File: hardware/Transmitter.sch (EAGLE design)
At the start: 2 parts, among them IC1 ATmega328P, U3 NRF24L01+

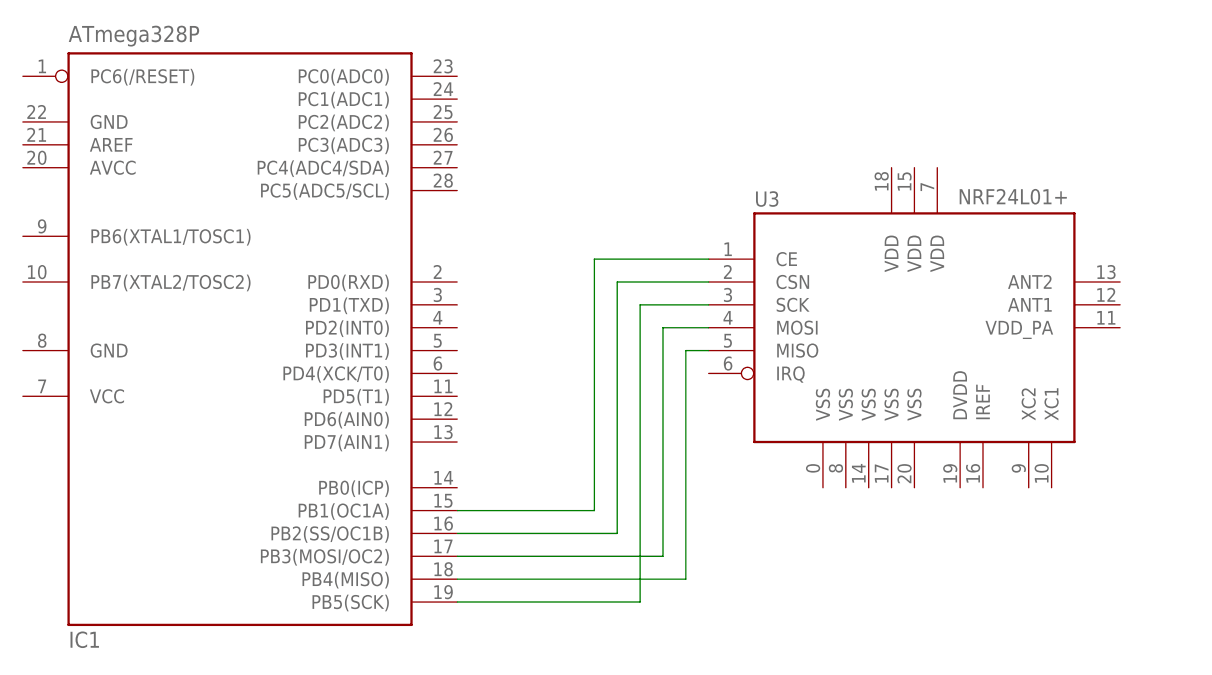
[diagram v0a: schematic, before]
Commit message: Added missing RESET/AVCC connections and eliminated short circuit in off switch
Resized schematics to conform image sizes
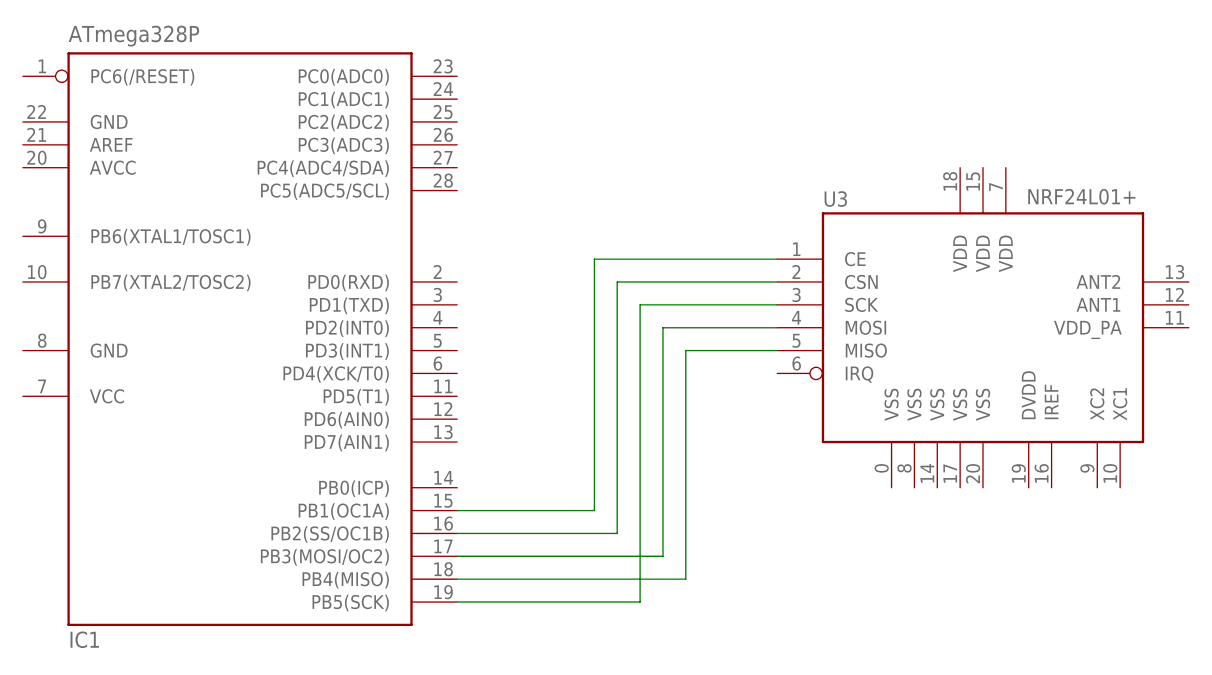
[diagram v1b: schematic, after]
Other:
- moved on the sheet: U3
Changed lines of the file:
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@@
 <instances>
 <instance part="IC1" gate="G$1" x="-7.62" y="38.1"/>
-<instance part="U3" gate="G$1" x="68.58" y="38.1" smashed="yes">
-<attribute name="NAME" x="50.8" y="51.562" size="1.6764" layer="95"/>
-<attribute name="VALUE" x="73.406" y="51.816" size="1.6764" layer="96"/>
+<instance part="U3" gate="G$1" x="76.2" y="38.1" smashed="yes">
+<attribute name="NAME" x="58.42" y="51.562" size="1.6764" layer="95"/>
+<attribute name="VALUE" x="81.026" y="51.816" size="1.6764" layer="96"/>
 </instance>
 </instances>
@@
 <segment>
 <pinref part="U3" gate="G$1" pin="CE"/>
-<wire x1="45.72" y1="45.72" x2="33.02" y2="45.72" width="0.1524" layer="91"/>
+<wire x1="53.34" y1="45.72" x2="33.02" y2="45.72" width="0.1524" layer="91"/>
 <wire x1="33.02" y1="45.72" x2="33.02" y2="17.78" width="0.1524" layer="91"/>
 <pinref part="IC1" gate="G$1" pin="PB1(OC1A)"/>
@@
 <segment>
 <pinref part="U3" gate="G$1" pin="CSN"/>
-<wire x1="45.72" y1="43.18" x2="35.56" y2="43.18" width="0.1524" layer="91"/>
+<wire x1="53.34" y1="43.18" x2="35.56" y2="43.18" width="0.1524" layer="91"/>
 <wire x1="35.56" y1="43.18" x2="35.56" y2="15.24" width="0.1524" layer="91"/>
 <pinref part="IC1" gate="G$1" pin="PB2(SS/OC1B)"/>
@@
 <segment>
 <pinref part="U3" gate="G$1" pin="SCK"/>
-<wire x1="45.72" y1="40.64" x2="38.1" y2="40.64" width="0.1524" layer="91"/>
+<wire x1="53.34" y1="40.64" x2="38.1" y2="40.64" width="0.1524" layer="91"/>
 <wire x1="38.1" y1="40.64" x2="38.1" y2="7.62" width="0.1524" layer="91"/>
 <pinref part="IC1" gate="G$1" pin="PB5(SCK)"/>
@@
 <segment>
 <pinref part="U3" gate="G$1" pin="MOSI"/>
-<wire x1="45.72" y1="38.1" x2="40.64" y2="38.1" width="0.1524" layer="91"/>
+<wire x1="53.34" y1="38.1" x2="40.64" y2="38.1" width="0.1524" layer="91"/>
 <wire x1="40.64" y1="38.1" x2="40.64" y2="12.7" width="0.1524" layer="91"/>
 <pinref part="IC1" gate="G$1" pin="PB3(MOSI/OC2)"/>
@@
 <segment>
 <pinref part="U3" gate="G$1" pin="MISO"/>
-<wire x1="45.72" y1="35.56" x2="43.18" y2="35.56" width="0.1524" layer="91"/>
+<wire x1="53.34" y1="35.56" x2="43.18" y2="35.56" width="0.1524" layer="91"/>
 <wire x1="43.18" y1="35.56" x2="43.18" y2="10.16" width="0.1524" layer="91"/>
 <pinref part="IC1" gate="G$1" pin="PB4(MISO)"/>
